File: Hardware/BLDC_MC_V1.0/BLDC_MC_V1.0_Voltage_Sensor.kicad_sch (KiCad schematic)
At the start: 23 parts, among them U12 TLV9061IDBVR, U13 TLV9061IDBVR, U14 TLV9061IDBVR, U15 TLV9061IDBVR

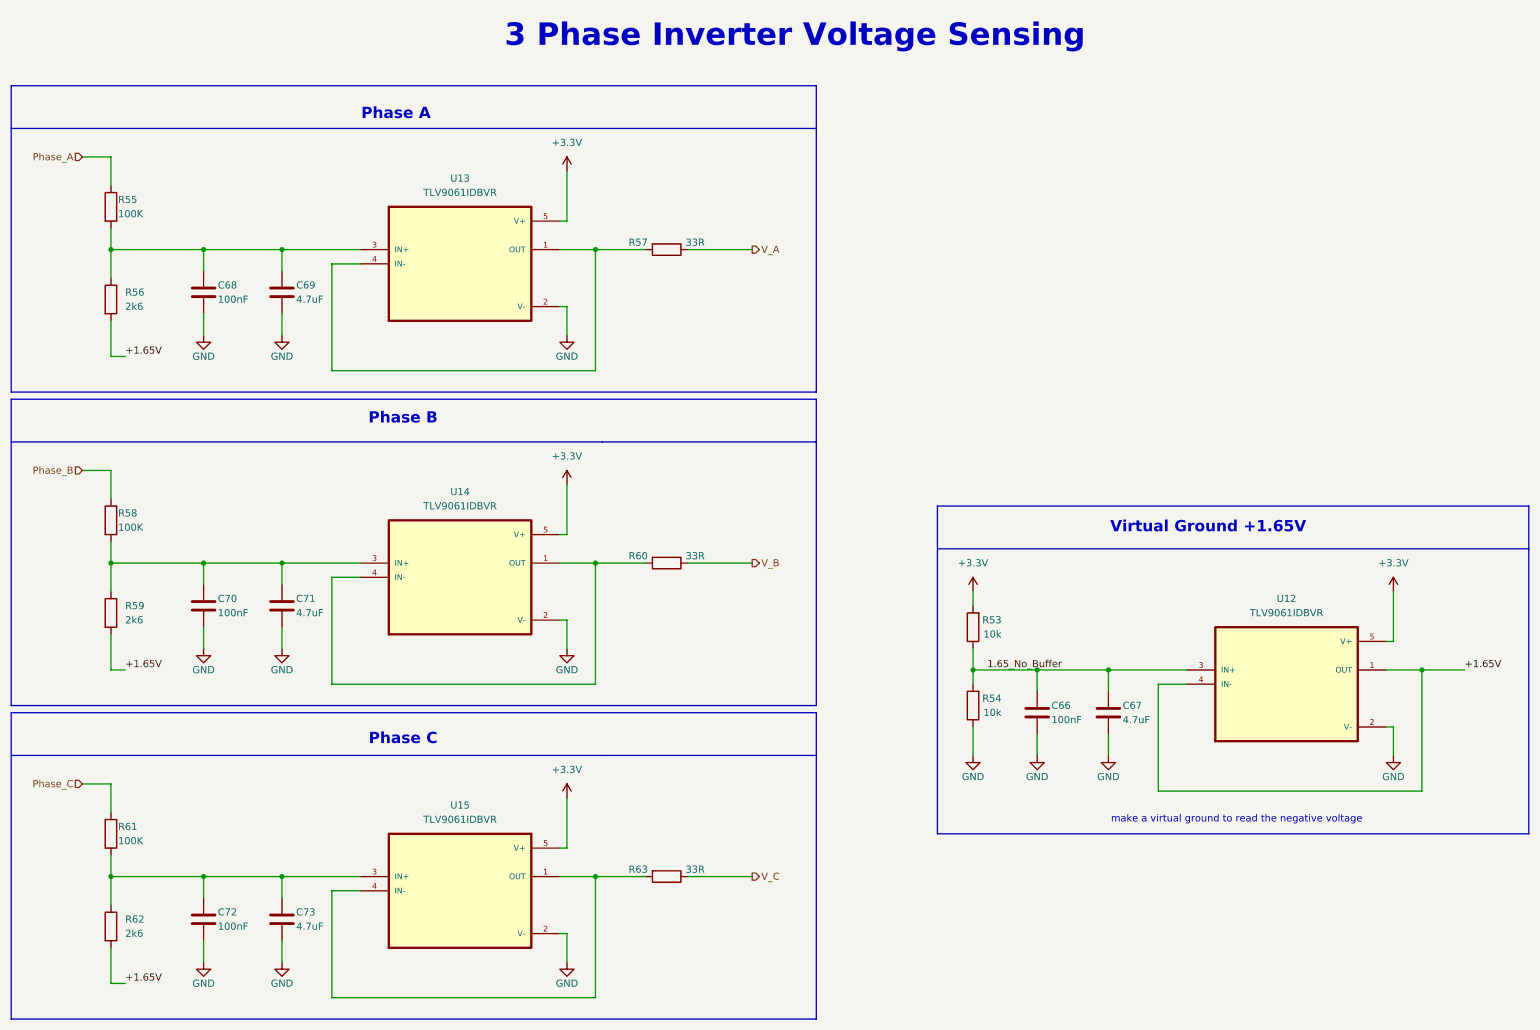
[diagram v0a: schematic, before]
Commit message: Edit the voltage sensor sheet by adding low pass filter
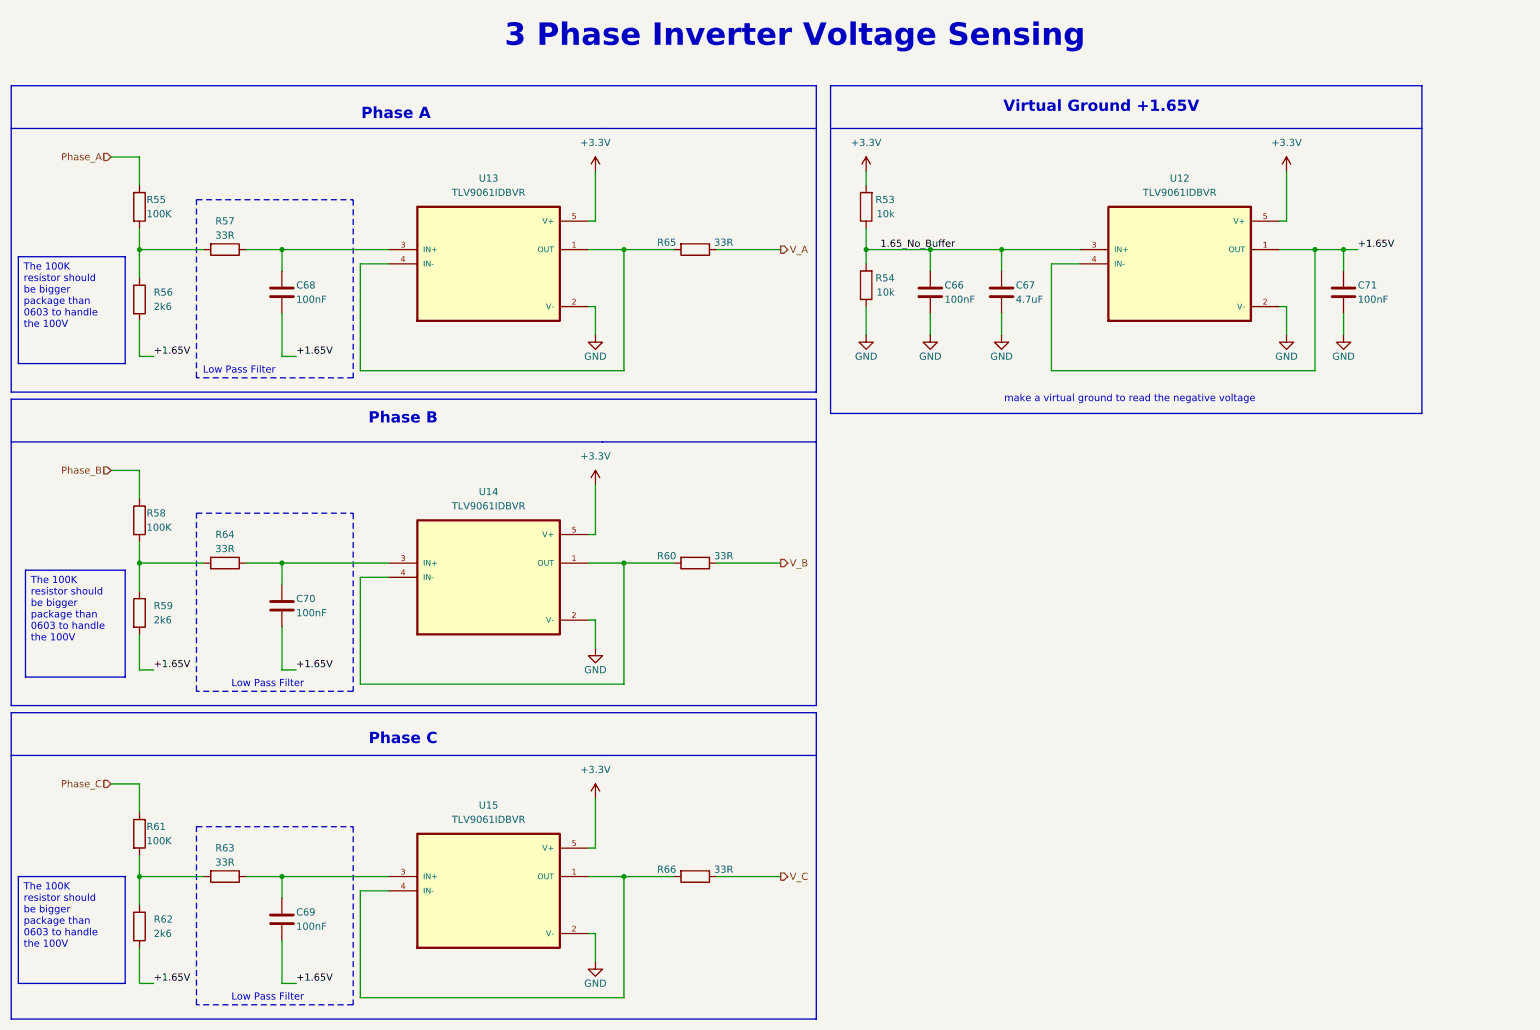
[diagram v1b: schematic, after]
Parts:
- removed C72: 100nF, Capacitor_SMD:C_0805_2012Metric, symbol Device:C
- removed C73: 4.7uF, Capacitor_SMD:C_1206_3216Metric, symbol Device:C
- added R64, R65, R66: 33R, Resistor_SMD:R_0603_1608Metric, symbol Device:R
- C69, C71: value 4.7uF -> 100nF; footprint Capacitor_SMD:C_1206_3216Metric -> Capacitor_SMD:C_0805_2012Metric; LCSC_PN C51205 -> C28233; MP CL31B475KBHNNNE -> CL21B104KCFNNNE
- R55, R58, R61: footprint Resistor_SMD:R_0603_1608Metric -> Resistor_SMD:R_1206_3216Metric; LCSC_PN C122538 -> C870633; MP RT0603BRD07100KL -> RT1206BRD072K7L
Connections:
- net +1.65V: now also C68.2, C69.2, C70.2, C71.1
- net GND: no longer C68.2, C69.2, C70.2
- net V_A: now also R65.1; no longer R57.1
- net V_C: now also R66.1; no longer R63.1
- net at U13.1 (OUT), U13.4 (IN-): now also R65.2; no longer R57.2
- net at R61.2, R62.1: now also R63.2; no longer U15.3 (IN+)
- net at U15.1 (OUT), U15.4 (IN-): now also R66.2; no longer R63.2
- new net: R55.2, R56.1, R57.2
- new net: C69.1, R63.1, U15.3 (IN+)
- new net: C68.1, R57.1, U13.3 (IN+)
- new net: C70.1, R64.1, U14.3 (IN+)
- new net: R58.2, R59.1, R64.2
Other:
- note added: "Low Pass Filter"
- moved on the sheet: C66, C67, C70, R53, R54, R59, R60, U12, U14
